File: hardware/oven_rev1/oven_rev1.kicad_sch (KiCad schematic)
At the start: 21 parts, among them J1 NEUTRAL, J10 SERIAL, J2 5V_IN, J3 RELAY_PWR, J4 LIVE, J5 OUTPUT, J6 RELAY_CTRL, J7 DISPLAY, J8 NUMPAD, J9 AVR-ISP-6, U1 ATmega328-AU, U2 MAX6675, Y1 16M

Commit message: Touched up title blocks and rev 3
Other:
- moved on the sheet: C2, C3, H1, H2, J1, J10, J2, J3, J4, J5, JP1, R1

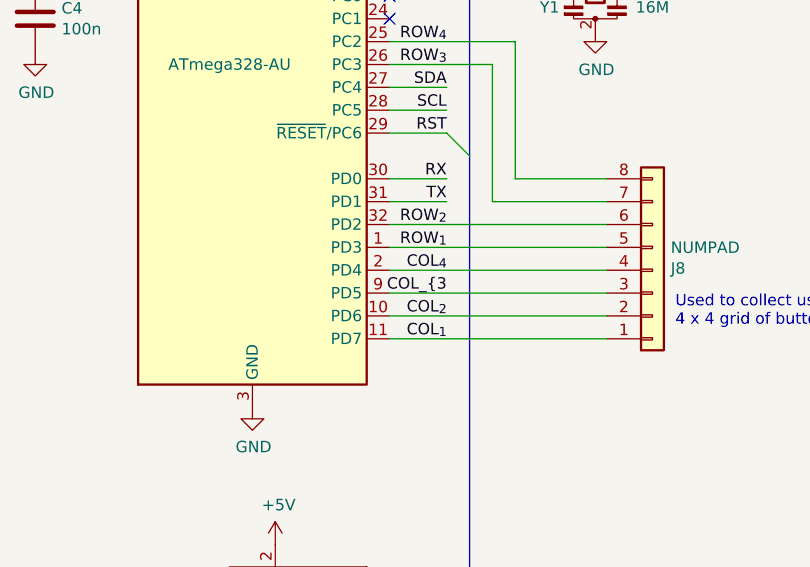
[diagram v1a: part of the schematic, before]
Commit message: Minor touchups for titleblocks
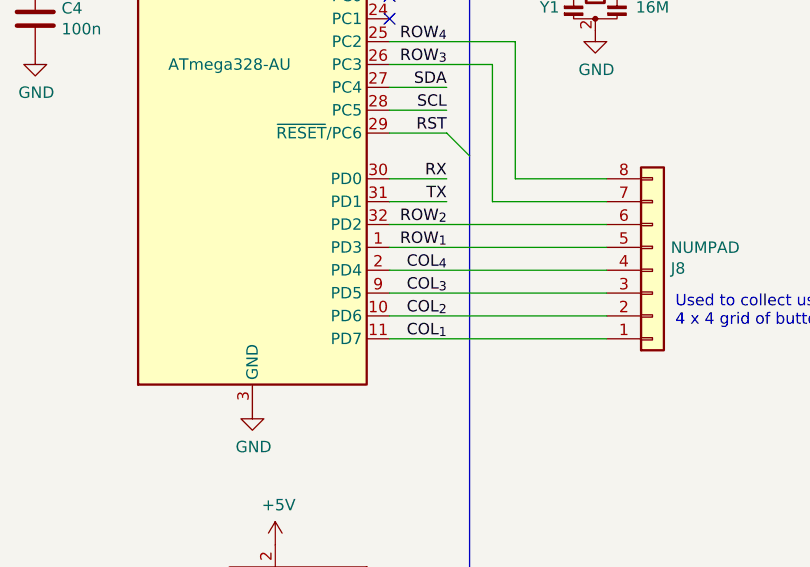
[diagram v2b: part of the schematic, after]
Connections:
- net COL_{3 renamed COL_{3}
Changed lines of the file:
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@@
     (effects (font (size 1.27 1.27)) (justify right bottom))
   )
-  (label "COL_{3" (at 67.31 90.17 180) (fields_autoplaced)
+  (label "COL_{3}" (at 67.31 90.17 180) (fields_autoplaced)
     (effects (font (size 1.27 1.27)) (justify right bottom))
   )
